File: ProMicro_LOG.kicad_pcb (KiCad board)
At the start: 2 copper layers, 17.8 x 30.5 mm, 17 parts, among them J1 Micro_SD_Card_Det, U1 DS3231MZ

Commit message: kicad-exports
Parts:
- removed TP2: initials, Symbol:initials
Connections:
- A1 pad 11: (no net) -> D8
- JP1 pad 2: D6 -> D8
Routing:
- net D8: track 0.00 -> 9.76 mm, vias 0 -> 1
- net D6: track 16.6 -> 15.3 mm
- net GND: vias 19 -> 18
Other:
- board text added: "nerdyscout.github.io/ProMicro_LOG"
- board text added: "v1.1"
- board text removed: "nerdyscout.github.io/ProMicro/LOG"
- board text removed: "v1.0"
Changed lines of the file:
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@@
-(kicad_pcb (version 20171130) (host pcbnew 5.1.5+dfsg1-2build2)
+(kicad_pcb (version 20171130) (host pcbnew 5.1.5)
   (general
     (thickness 0.8)
     (drawings 10)
-    (tracks 157)
+    (tracks 162)
     (zones 0)
-    (modules 17)
-    (nets 18)
+    (modules 16)
+    (nets 19)
   )
   (page A4)
   (title_block
-    (title http://github.com/nerdyscout/ProMicro_LOG)
+    (title ProMicro_LOG)
     (date 2020-07-13)
     (rev v1.0)
@@
     (0 F.Cu mixed)
     (31 B.Cu mixed)
-    (32 B.Adhes user hide)
-    (33 F.Adhes user hide)
-    (34 B.Paste user hide)
-    (35 F.Paste user hide)
+    (32 B.Adhes user)
+    (33 F.Adhes user)
+    (34 B.Paste user)
+    (35 F.Paste user)
     (36 B.SilkS user)
     (37 F.SilkS user)
     (38 B.Mask user)
-    (39 F.Mask user hide)
+    (39 F.Mask user)
     (40 Dwgs.User user)
     (41 Cmts.User user)
@@
   (net 16 "Net-(D1-Pad2)")
   (net 17 D6)
+  (net 18 D8)
   (net_class Default "This is the default net class."
     (clearance 0.2)
@@
     (add_net D3)
     (add_net D6)
+    (add_net D8)
     (add_net D9)
     (add_net "Net-(D1-Pad2)")
@@
       (xy 0.555814 2.531069)) (layer B.SilkS) (width 0.01))
   )
-  (module Symbol:initials (layer F.Cu)
-    (at 145.415 77.47)
-    (fp_text reference TP2 (at 0 0) (layer F.SilkS) hide
-      (effects (font (size 1.524 1.524) (thickness 0.3)))
-    )
-    (fp_text value initials (at 0.75 0) (layer F.SilkS) hide
-      (effects (font (size 1.524 1.524) (thickness 0.3)))
-    )
-    (fp_poly (pts (xy 0.703956 -1.785244) (xy 0.729378 -1.665482) (xy 0.705735 -1.454342) (xy 0.690198 -1.386603)
-      (xy 0.63935 -1.132969) (xy 0.587603 -0.786438) (xy 0.547035 -0.430489) (xy 0.488 0.197356)
-      (xy 0.721085 0.014011) (xy 1.009772 -0.147205) (xy 1.24742 -0.155244) (xy 1.41502 -0.023202)
-      (xy 1.493563 0.235821) (xy 1.477895 0.535505) (xy 1.401001 0.872557) (xy 1.288485 1.222888)
-      (xy 1.163312 1.52202) (xy 1.070085 1.680375) (xy 0.984201 1.725181) (xy 0.924698 1.644827)
-      (xy 0.905077 1.482996) (xy 0.938841 1.283371) (xy 0.943248 1.27) (xy 1.020121 0.999101)
-      (xy 1.079596 0.707538) (xy 1.114394 0.445394) (xy 1.117237 0.262754) (xy 1.097353 0.209619)
-      (xy 0.99817 0.237731) (xy 0.843432 0.369851) (xy 0.667556 0.566533) (xy 0.504956 0.788333)
-      (xy 0.390048 0.995803) (xy 0.373213 1.039603) (xy 0.277472 1.224511) (xy 0.166933 1.312586)
-      (xy 0.155668 1.313746) (xy 0.000667 1.358816) (xy -0.198847 1.46549) (xy -0.202344 1.467773)
-      (xy -0.401822 1.576882) (xy -0.664543 1.694735) (xy -0.928077 1.796162) (xy -1.129994 1.855994)
-      (xy -1.181867 1.862667) (xy -1.292384 1.811803) (xy -1.297847 1.806597) (xy -1.2649 1.741503)
-      (xy -1.115425 1.644819) (xy -1.036792 1.606405) (xy -0.787974 1.467219) (xy -0.546309 1.290379)
-      (xy -0.355291 1.112615) (xy -0.258414 0.970656) (xy -0.254 0.945352) (xy -0.327922 0.879759)
-      (xy -0.520011 0.788828) (xy -0.740834 0.708475) (xy -1.06895 0.570519) (xy -1.236478 0.408428)
-      (xy -1.252161 0.199031) (xy -1.124741 -0.080847) (xy -1.070695 -0.16584) (xy -0.889576 -0.373961)
-      (xy -0.650525 -0.565088) (xy -0.395776 -0.715301) (xy -0.167563 -0.800683) (xy -0.00812 -0.797316)
-      (xy 0.01511 -0.780756) (xy 0.017302 -0.692427) (xy -0.138598 -0.58102) (xy -0.207656 -0.546562)
-      (xy -0.446115 -0.394009) (xy -0.666146 -0.188201) (xy -0.832638 0.029015) (xy -0.910481 0.215789)
-      (xy -0.90515 0.284779) (xy -0.799353 0.374554) (xy -0.593731 0.449709) (xy -0.535927 0.46214)
-      (xy -0.284165 0.534882) (xy -0.087821 0.635205) (xy -0.067499 0.651668) (xy 0.043502 0.730076)
-      (xy 0.096478 0.669994) (xy 0.117536 0.581004) (xy 0.176382 0.235248) (xy 0.207892 -0.072514)
-      (xy 0.210111 -0.303137) (xy 0.181083 -0.417476) (xy 0.167713 -0.423333) (xy 0.094027 -0.491934)
-      (xy 0.084667 -0.550333) (xy 0.125578 -0.663074) (xy 0.160287 -0.677333) (xy 0.212934 -0.753652)
-      (xy 0.275323 -0.952672) (xy 0.328068 -1.200544) (xy 0.413762 -1.555727) (xy 0.51738 -1.768019)
-      (xy 0.63238 -1.827245) (xy 0.703956 -1.785244)) (layer F.SilkS) (width 0.01))
-  )
   (module Module:Sparkfun_Pro_Micro (layer F.Cu)
     (at 137.16 76.2)
@@
     (pad 21 thru_hole oval (at 15.24 7.62) (size 1.6 1.6) (drill 1) (layers *.Cu *.Mask)
       (net 2 +3V3))
-    (pad 11 thru_hole oval (at 0 25.4) (size 1.6 1.6) (drill 1) (layers *.Cu *.Mask))
+    (pad 11 thru_hole oval (at 0 25.4) (size 1.6 1.6) (drill 1) (layers *.Cu *.Mask)
+      (net 18 D8))
     (pad 20 thru_hole oval (at 15.24 10.16) (size 1.6 1.6) (drill 1) (layers *.Cu *.Mask))
     (pad 10 thru_hole oval (at 0 22.86) (size 1.6 1.6) (drill 1) (layers *.Cu *.Mask))
@@
     (fp_arc (start 0.7 -0.3) (end 1.4 -0.3) (angle -90) (layer F.SilkS) (width 0.12))
     (pad 2 smd custom (at 0.65 0 270) (size 1 0.5) (layers F.Cu F.Mask)
-      (net 17 D6) (zone_connect 2)
+      (net 18 D8) (zone_connect 2)
       (options (clearance outline) (anchor rect))
       (primitives
@@
     )
   )
-  (gr_text v1.0 (at 142.24 100.33 90) (layer B.SilkS)
+  (gr_text v1.1 (at 142.24 100.33 90) (layer B.SilkS)
     (effects (font (size 0.9 0.9) (thickness 0.2)) (justify mirror))
   )
-  (gr_text nerdyscout.github.io/ProMicro/LOG (at 139.7 90.17 90) (layer B.SilkS)
+  (gr_text nerdyscout.github.io/ProMicro_LOG (at 139.7 90.17 90) (layer B.SilkS)
     (effects (font (size 1 1) (thickness 0.25)) (justify mirror))
   )
@@
   (via (at 139.954 89.789) (size 0.5) (drill 0.2) (layers F.Cu B.Cu) (net 1))
   (via (at 147.193 84.455) (size 0.5) (drill 0.2) (layers F.Cu B.Cu) (net 1))
-  (via (at 144.145 103.505) (size 0.5) (drill 0.2) (layers F.Cu B.Cu) (net 1))
   (via (at 141.605 104.14) (size 0.5) (drill 0.2) (layers F.Cu B.Cu) (net 1))
   (via (at 141.605 90.17) (size 0.5) (drill 0.2) (layers F.Cu B.Cu) (net 1))
@@
   (segment (start 148.59 93.8275) (end 149.4535 93.8275) (width 0.25) (layer F.Cu) (net 16))
   (segment (start 150.495 93.8275) (end 149.4535 93.8275) (width 0.25) (layer F.Cu) (net 16))
-  (segment (start 145.415 104.155) (end 146.7 104.155) (width 0.25) (layer F.Cu) (net 17))
   (via (at 146.7 104.155) (size 0.5) (drill 0.2) (layers F.Cu B.Cu) (net 17))
   (segment (start 149.225 104.2925) (end 147.4725 104.2925) (width 0.25) (layer F.Cu) (net 17))
@@
   (segment (start 139.065 96.52) (end 146.7 104.155) (width 0.25) (layer B.Cu) (net 17))
   (segment (start 137.16 96.52) (end 139.065 96.52) (width 0.25) (layer B.Cu) (net 17))
+  (via (at 144.145 102.87) (size 0.5) (drill 0.2) (layers F.Cu B.Cu) (net 18))
+  (segment (start 142.875 101.6) (end 144.145 102.87) (width 0.25) (layer B.Cu) (net 18))
+  (segment (start 137.16 101.6) (end 142.875 101.6) (width 0.25) (layer B.Cu) (net 18))
+  (segment (start 144.145 102.87) (end 144.145 103.505) (width 0.25) (layer F.Cu) (net 18))
+  (segment (start 144.145 103.632592) (end 144.145 103.505) (width 0.25) (layer F.Cu) (net 18))
+  (segment (start 144.667408 104.155) (end 144.145 103.632592) (width 0.25) (layer F.Cu) (net 18))
+  (segment (start 145.415 104.155) (end 144.667408 104.155) (width 0.25) (layer F.Cu) (net 18))
   (zone (net 1) (net_name GND) (layer B.Cu) (hatch edge 0.508)
     (connect_pads (clearance 0.125))

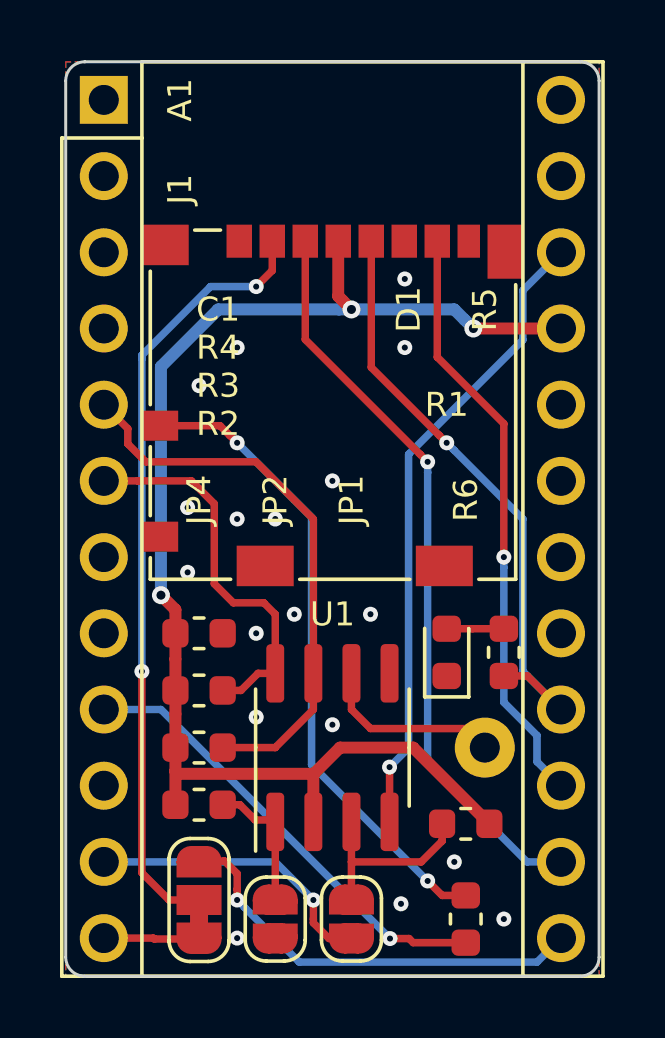
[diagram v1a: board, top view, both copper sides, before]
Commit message: fixed missing TRG
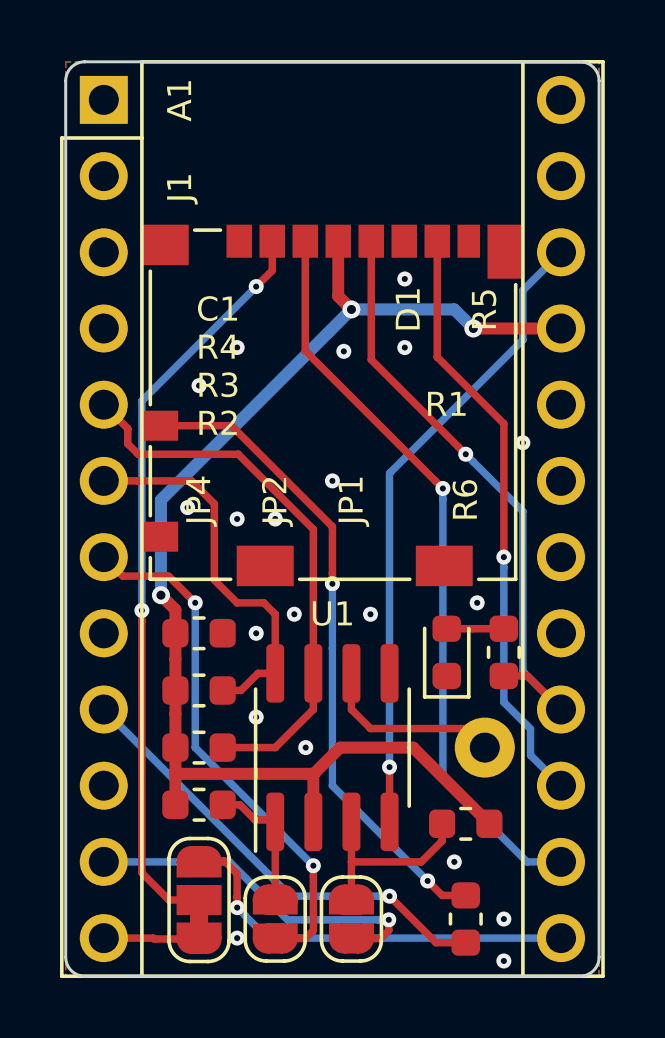
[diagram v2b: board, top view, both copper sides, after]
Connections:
- net D10 renamed CS0
- net D14 renamed CIPO
- net D15 renamed SCK
- net D16 renamed COPI
- net D2 renamed SDA
- net D3 renamed SCL
- net D6 renamed BTN
- net D8 renamed INT
- net D9 renamed CS1
- A1 pad 7: (no net) -> TRG
- JP2 pad 2: (no net) -> TRG
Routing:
- net TRG: track 0.00 -> 17.6 mm, vias 0 -> 2
- net +3V3: track 45.2 -> 42.6 mm
- net INT: track 9.76 -> 12.0 mm
- net CS: track 26.0 -> 25.1 mm
- net CS0: track 14.3 -> 13.8 mm
- net GND: vias 18 -> 20
